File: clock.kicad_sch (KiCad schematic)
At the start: 32 parts, among them P16 SMA, P2 SMA, U19 SI5351C, U30 74LVC1G3157, U31 74LVC1G3157, U33 74HC4051, X1 TCXO

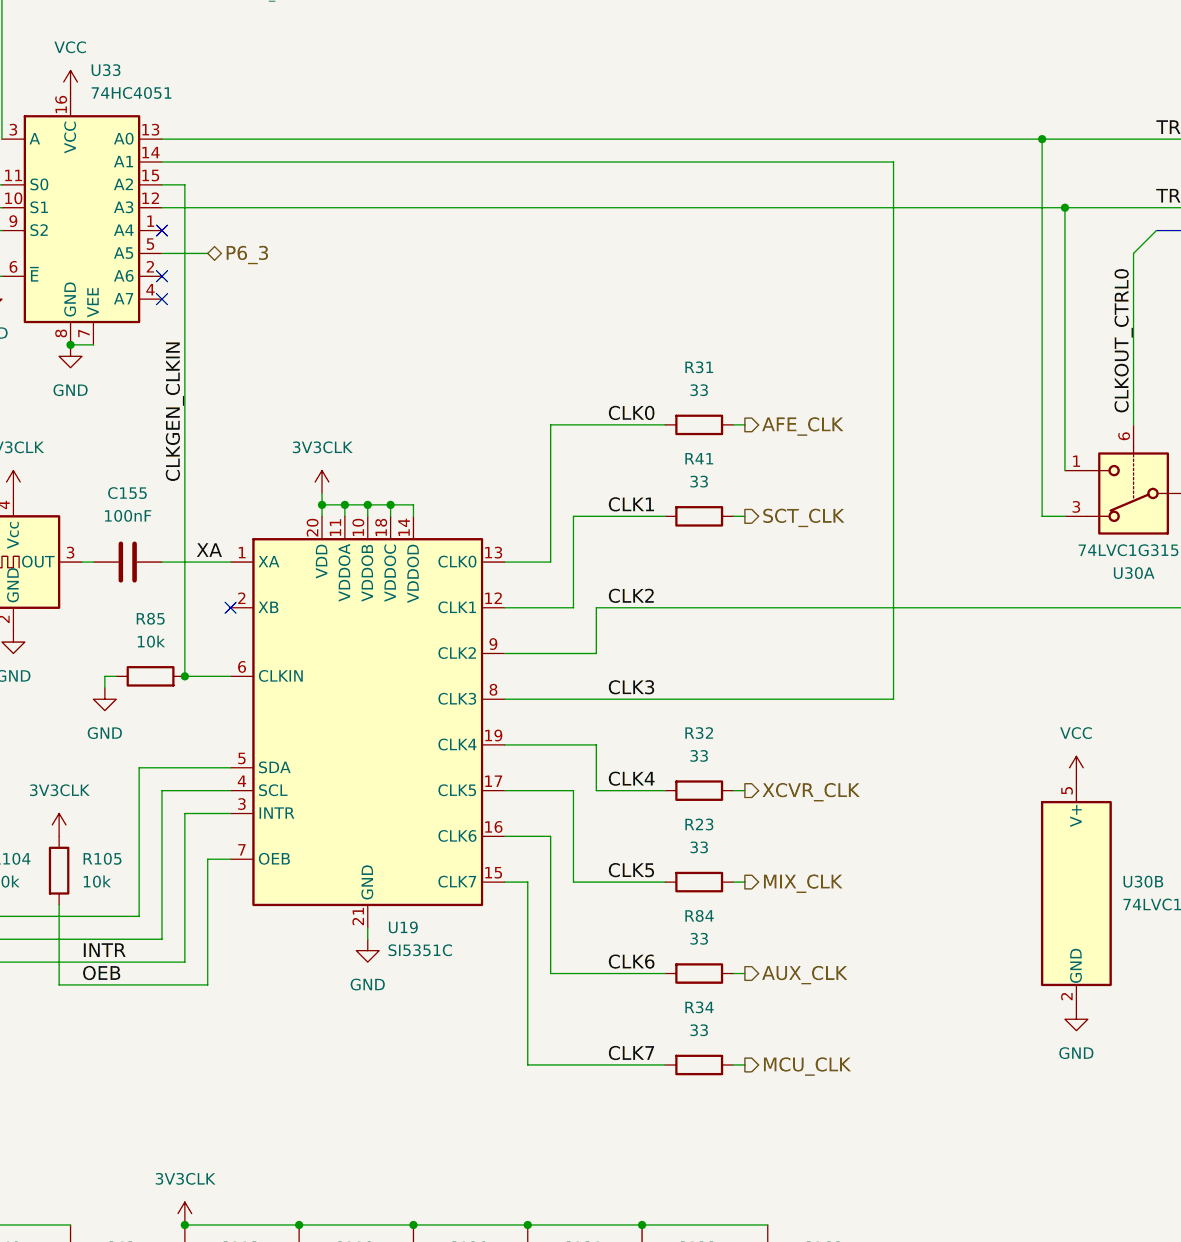
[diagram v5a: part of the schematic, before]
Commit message: Add test points
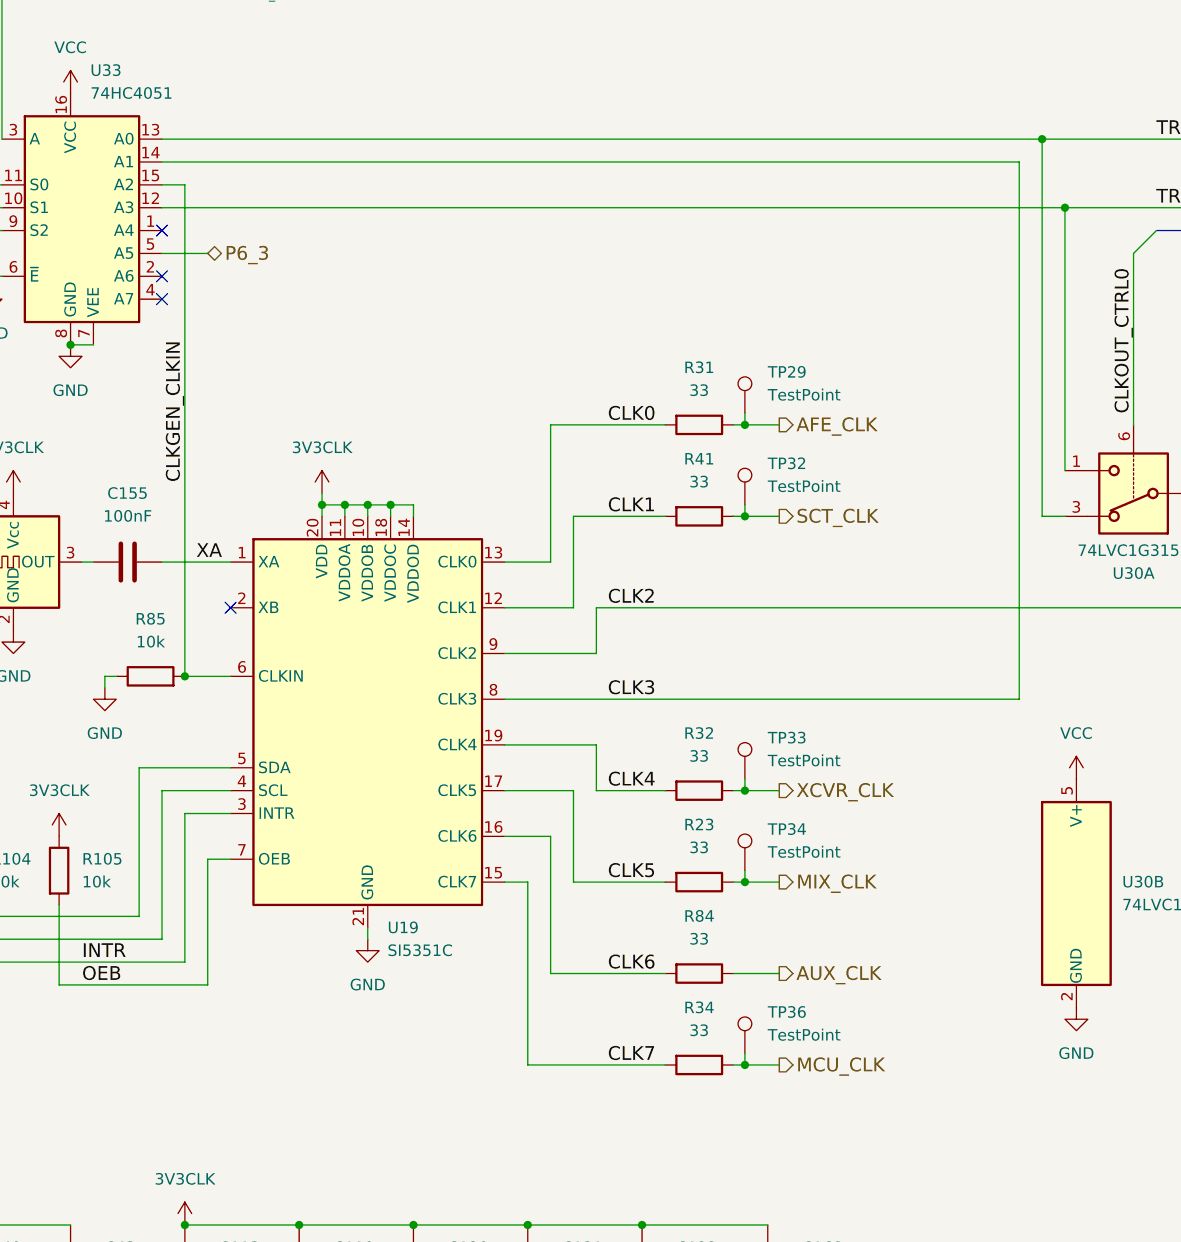
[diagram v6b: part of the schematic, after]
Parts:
- added TP29, TP32, TP33, TP34, TP36: TestPoint, TestPoint:TestPoint_Pad_D1.0mm, symbol Connector:TestPoint
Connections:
- net AFE_CLK: now also TP29.1
- net MCU_CLK: now also TP36.1
- net MIX_CLK: now also TP34.1
- net SCT_CLK: now also TP32.1
- net XCVR_CLK: now also TP33.1

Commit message: Use consistent footprints for 0402 and 0201 diodes
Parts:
- D3, D9: footprint praline:DFN1006-2 -> praline:TSLP-2-19
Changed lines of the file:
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@@
 			)
 		)
-		(property "Footprint" "praline:DFN1006-2"
+		(property "Footprint" "praline:TSLP-2-19"
 			(at 50.8 39.37 0)
 			(effects
@@
 			)
 		)
-		(property "Footprint" "praline:DFN1006-2"
+		(property "Footprint" "praline:TSLP-2-19"
 			(at 247.65 102.87 0)
 			(effects

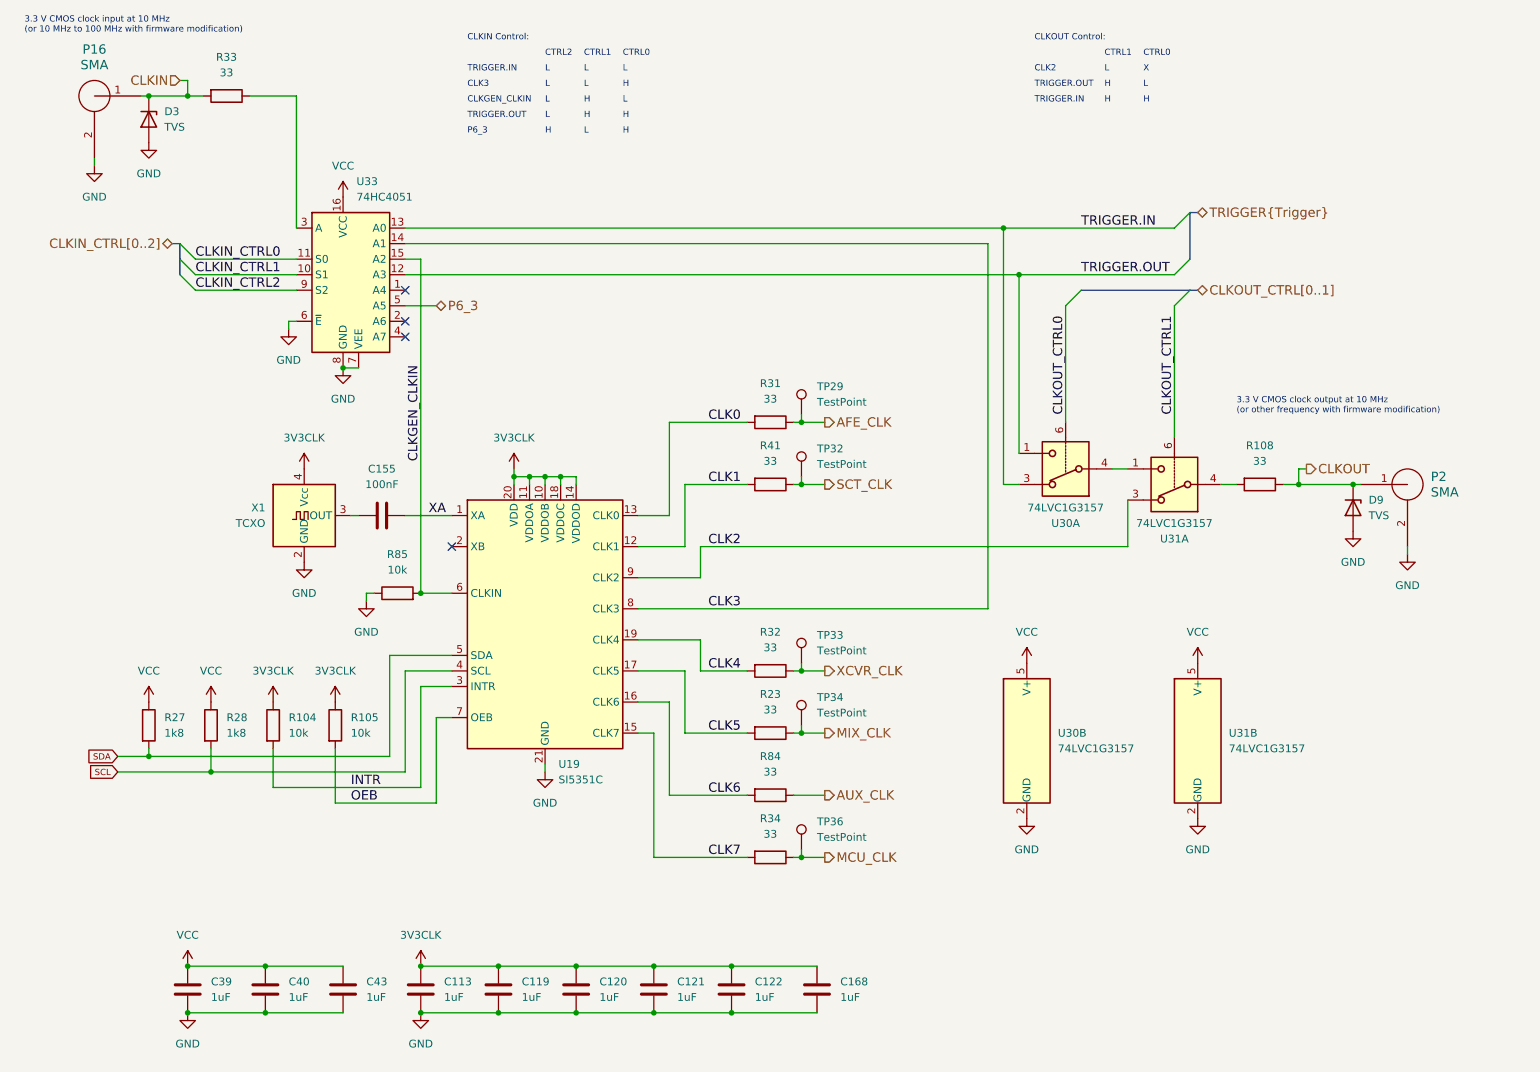
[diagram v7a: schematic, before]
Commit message: Add FPGA_CLK clock generator output
- Remove TRIGGER_EN signal, to be replaced with SPI command
- Reassign clock generator outputs for CLKOUT and CLKIN
- Reassign various FPGA pins
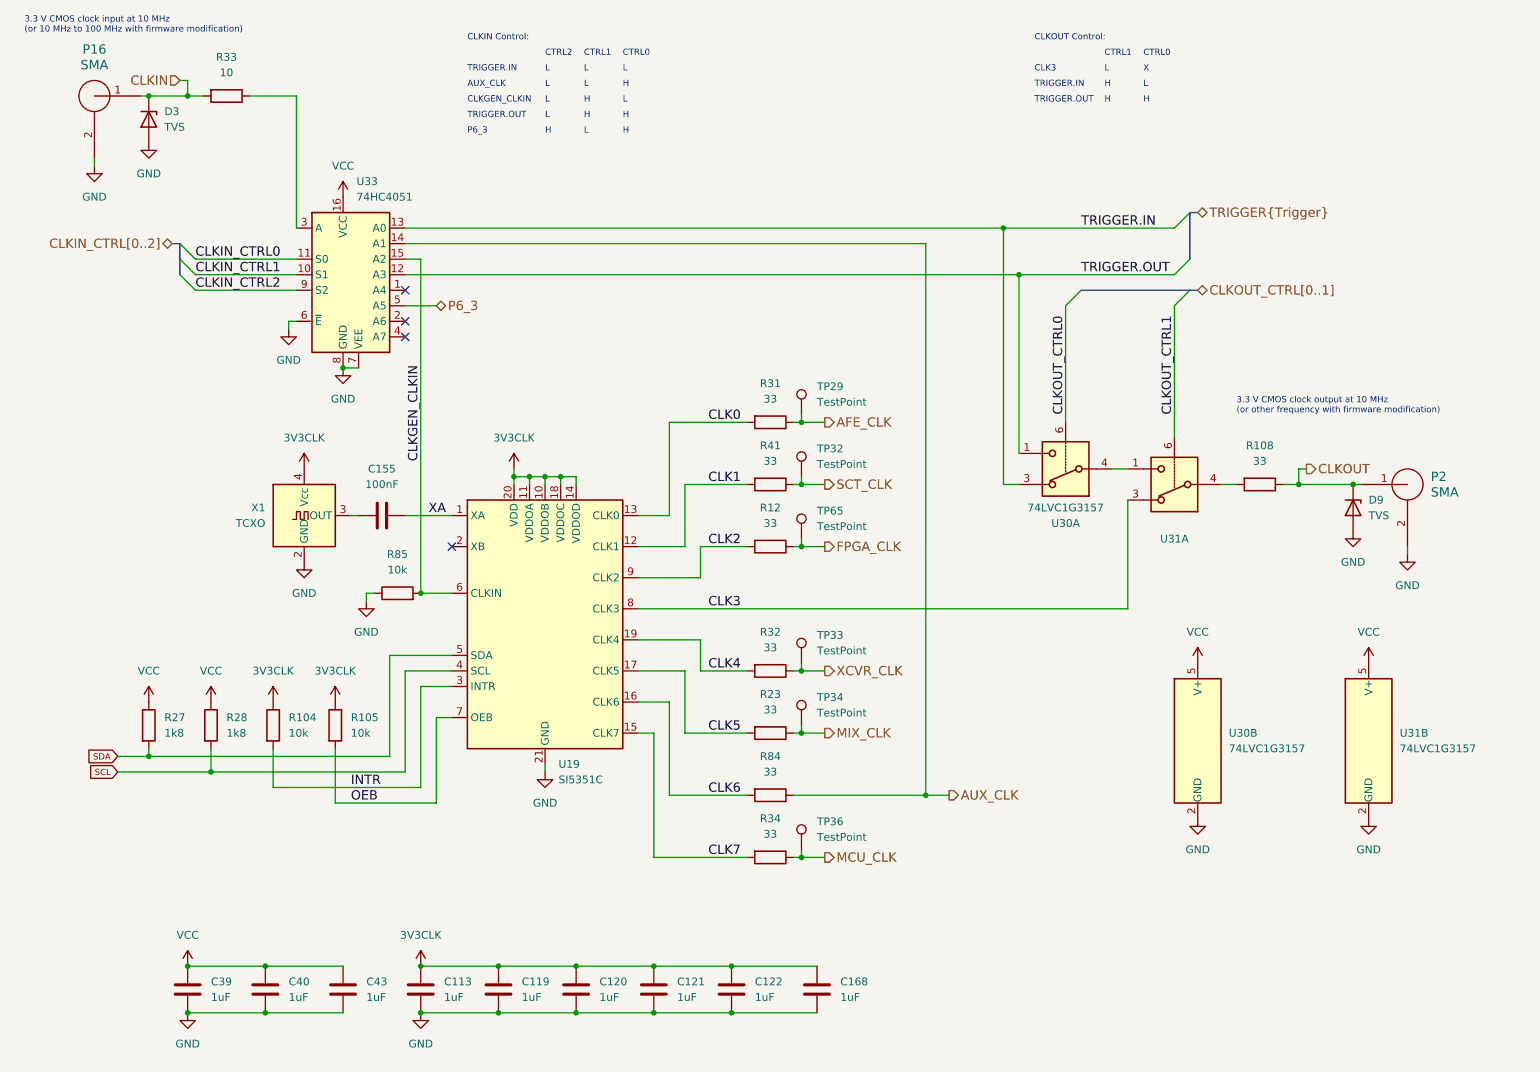
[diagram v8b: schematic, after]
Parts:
- added R12: 33, Resistor_SMD:R_0402_1005Metric, symbol Device:R
- added TP65: TestPoint, TestPoint:TestPoint_Pad_D1.0mm, symbol Connector:TestPoint
- R33: value 33 -> 10; footprint Resistor_SMD:R_0402_1005Metric -> Resistor_SMD:R_0201_0603Metric; Part Number RC0402JR-0733RL -> RC0201JR-0710RL
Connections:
- net AUX_CLK: now also U33.14 (A1)
- net CLK2: now also R12.2; no longer U31.3
- net CLK3: now also U31.3; no longer U33.14 (A1)
- new net FPGA_CLK: R12.1, TP65.1
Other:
- note added: "AUX_CLK"
- note removed: "CLK2"
- moved on the sheet: U30B, U31B
